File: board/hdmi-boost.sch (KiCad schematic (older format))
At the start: 15 parts, among them P1 PMOD-Device-x2-Type-XHS-Alt, U31 XC9140, U32 REG710-DBV

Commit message: Working on things.
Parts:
- removed P1: PMOD-Device-x2-Type-XHS-Alt, pmod-conn_6x2:pmod_pin_array_6x2, symbol PMOD-Device-x2-Type-XHS-Alt
- added CTX? (x16): 0.1uF, Capacitors_SMD:C_0402, symbol hdmi-boost-rescue:C_Small
- added CTX?: 10n, Capacitors_SMD:C_0402, symbol hdmi-boost-rescue:C_Small
- added CTX? (x4): 0.1uF, Capacitors_SMD:C_0402, symbol hdmi-boost-rescue:C
- added DTX?: D, Diodes_SMD:SOD-523, symbol hdmi-boost-rescue:D
- added J? (x2): HDMI_IN, symbol hdmi-boost-rescue:HDMI_IN
- added JTX? (x2): HDMI_OUT, hdmi:HDMI_TH, symbol hdmi-boost-rescue:HDMI_OUT
- added PTX?: PMOD-CONN_6X2, pmod:pmod_pin_array_6x2, symbol hdmi-boost-rescue:PMOD-CONN_6X2
- added R? (x2): R_Shunt_US, symbol Device:R_Shunt_US
- added RTX?: 27K, Resistors_SMD:R_0402, symbol hdmi-boost-rescue:R
- added RTX? (x4): 2k2, Resistors_SMD:R_0402, symbol hdmi-boost-rescue:R
- added RTX?: 12k4, Resistors_SMD:R_0402, symbol hdmi-boost-rescue:R
- added URX0, UTX0: PTN3363, Housings_DFN_QFN:QFN-32-1EP_5x5mm_Pitch0.5mm, symbol hdmi-boost-rescue:PTN3363
- C311, C322, CV5: symbol C -> hdmi-boost-rescue:C
- C321: symbol C_Small -> hdmi-boost-rescue:C_Small
- L31: symbol INDUCTOR -> hdmi-boost-rescue:INDUCTOR
- R31, R32, RDC1, RDE1, REQ0, REQ1, ROE1: symbol R -> hdmi-boost-rescue:R
- U31: symbol XC9140 -> hdmi-boost-rescue:XC9140
- U32: symbol REG710-DBV -> hdmi-boost-rescue:REG710-DBV
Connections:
- net labels added: HDMIA_RX0_CLK+, HDMIA_RX0_CLK-, HDMIA_RX0_D0+, HDMIA_RX0_D0-, HDMIA_RX0_D1+, HDMIA_RX0_D1-, HDMIA_RX0_D2+, HDMIA_RX0_D2-, HDMIA_TX0_CLK+, HDMIA_TX0_CLK-, HDMIA_TX0_D0+, HDMIA_TX0_D0-, HDMIA_TX0_D1+, HDMIA_TX0_D1-, HDMIA_TX0_D2+, HDMIA_TX0_D2-, HDMIP_RX0_CLK+, HDMIP_RX0_CLK-, HDMIP_RX0_D0+, HDMIP_RX0_D0-, HDMIP_RX0_D1+, HDMIP_RX0_D1-, HDMIP_RX0_D2+, HDMIP_RX0_D2-, HDMIP_RX0_HOT, HDMIP_RX0_SCL, HDMIP_RX0_SDA, HDMIP_TX0_CLK+, HDMIP_TX0_CLK-, HDMIP_TX0_D0+, HDMIP_TX0_D0-, HDMIP_TX0_D1+, HDMIP_TX0_D1-, HDMIP_TX0_D2+, HDMIP_TX0_D2-, HDMIP_TX0_HOT, HDMIP_TX0_SCL, HDMIP_TX0_SDA, HDMI_RX0_CEC, HDMI_TX0_DDC_EN, RX05V0
- wire segments 91 -> 290
- no-connect marks 0 -> 2
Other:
- note added: "Opsis Side"
- note added: "← From Presentor Computer"
- note added: "→ To Long Distance Display"
- note removed: "HDMI High Speed Signals"

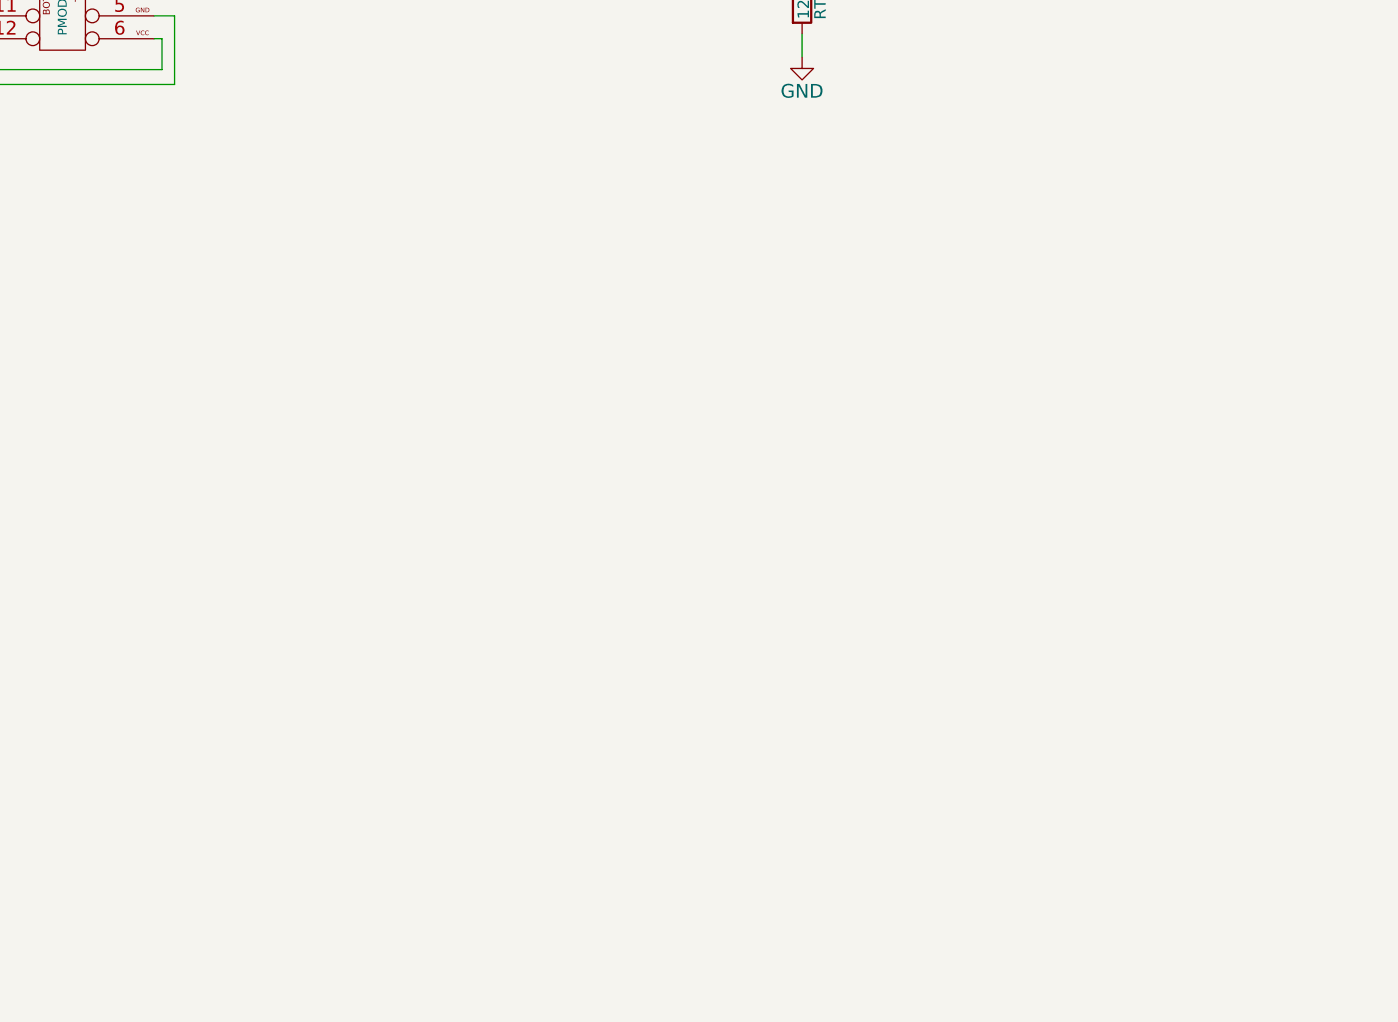
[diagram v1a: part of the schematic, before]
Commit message: Adding efm32hg309 part.
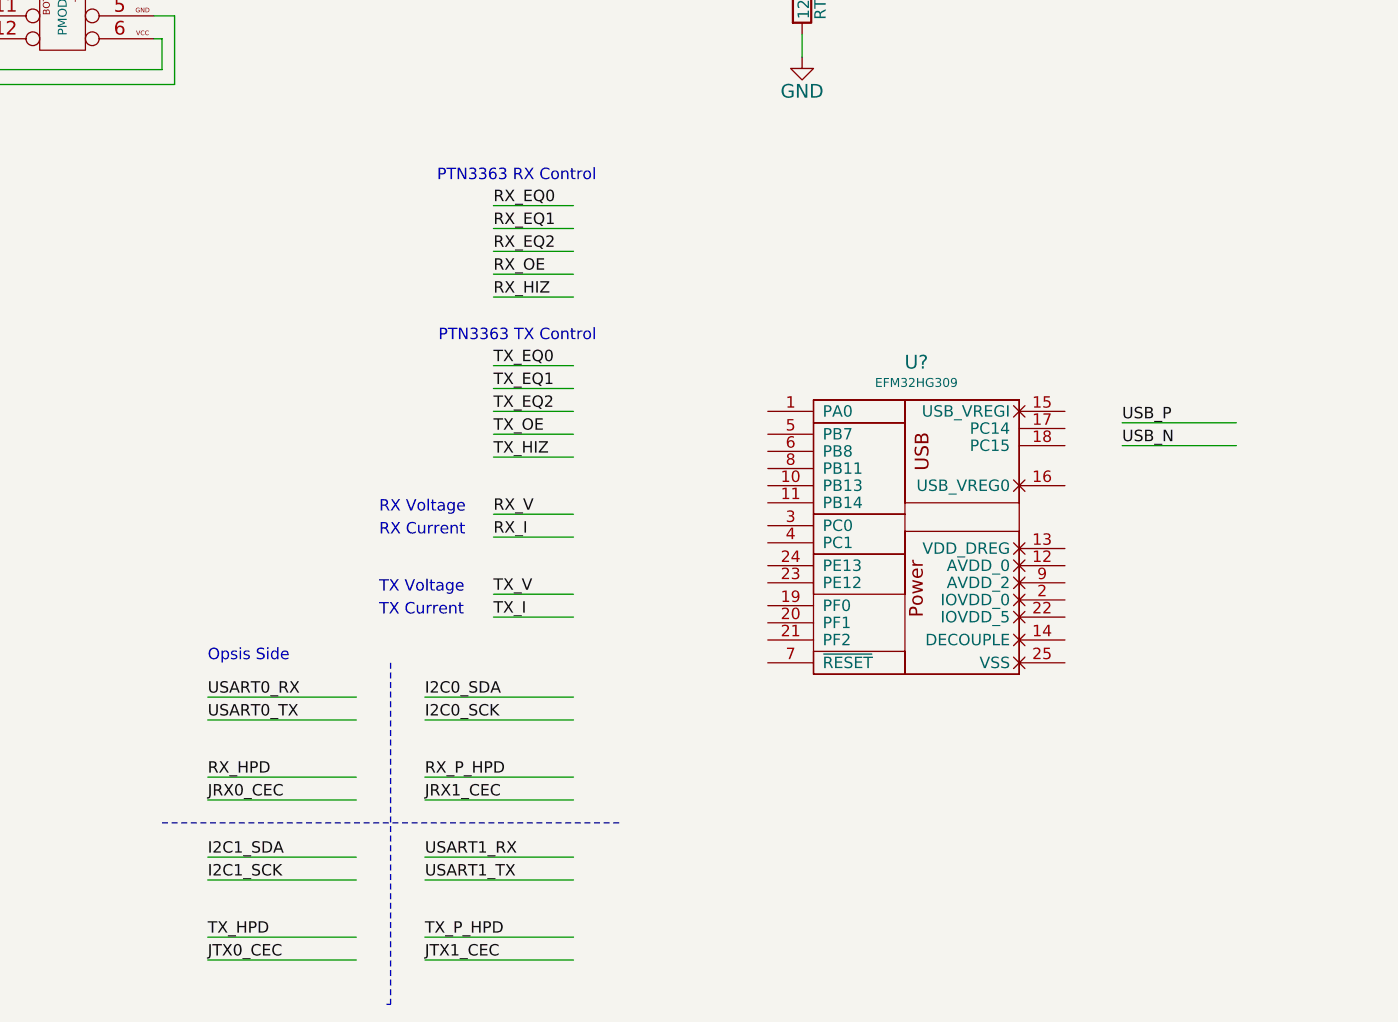
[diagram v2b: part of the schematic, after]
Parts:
- added U?: EFM32HG309, symbol efm32hg309:EFM32HG309
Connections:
- net labels added: I2C0_SCK, I2C0_SDA, I2C1_SCK, I2C1_SDA, JRX0_CEC, JRX1_CEC, JTX0_CEC, JTX1_CEC, RX_EQ0, RX_EQ1, RX_EQ2, RX_HIZ, RX_HPD, RX_I, RX_OE, RX_P_HPD, RX_V, TX_EQ0, TX_EQ1, TX_EQ2, TX_HIZ, TX_HPD, TX_I, TX_OE, TX_P_HPD, TX_V, USART0_RX, USART0_TX, USART1_RX, USART1_TX, USB_N, USB_P
- wire segments 290 -> 322
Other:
- note added: "PTN3363 RX Control"
- note added: "PTN3363 TX Control"
- note added: "RX Current"
- note added: "RX Voltage\n"
- note added: "TX Current"
- note added: "TX Voltage"
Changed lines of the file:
@@
 	25800 8300 25800 8500
 Connection ~ 25800 8300
+$Comp
+L efm32hg309:EFM32HG309 U?
+U 1 1 5E199B4B
+P 16000 8100
+F 0 "U?" H 16450 9465 60  0000 C CNN
+F 1 "EFM32HG309" H 16450 9375 39  0000 C CNN
+F 2 "" H 16000 8100 60  0000 C CNN
+F 3 "" H 16000 8100 60  0000 C CNN
+	1    16000 8100
+	1    0    0    -1
+$EndComp
+Wire Wire Line
+	14000 8200 13350 8200
+Wire Wire Line
+	14000 8300 13350 8300
+Text Label 13350 8200 0    50   ~ 0
+USART0_RX
+Text Label 13350 8300 0    50   ~ 0
+USART0_TX
+Wire Wire Line
+	14950 8900 14300 8900
+Wire Wire Line
+	14300 9000 14950 9000
+Text Label 14300 8900 0    50   ~ 0
+USART1_RX
+Text Label 14300 9000 0    50   ~ 0
+USART1_TX
+Wire Wire Line
+	14950 8200 14300 8200
+Wire Wire Line
+	14300 8300 14950 8300
+Wire Wire Line
+	14000 8900 13350 8900
+Wire Wire Line
+	13350 9000 14000 9000
+Text Label 14300 8200 0    50   ~ 0
+I2C0_SDA
+Text Label 14300 8300 0    50   ~ 0
+I2C0_SCK
+Text Label 13350 8900 0    50   ~ 0
+I2C1_SDA
+Text Label 13350 9000 0    50   ~ 0
+I2C1_SCK
+Wire Wire Line
+	17350 7000 17850 7000
+Wire Wire Line
+	17350 7100 17850 7100
+Text Label 17350 7000 0    50   ~ 0
+USB_P
+Text Label 17350 7100 0    50   ~ 0
+USB_N
+Wire Wire Line
+	14950 7400 14600 7400
+Wire Wire Line
+	14600 7500 14950 7500
+Wire Wire Line
+	14600 7750 14950 7750
+Wire Wire Line
+	14600 7850 14950 7850
+Text Label 14600 7400 0    50   ~ 0
+RX_V
+Text Label 14600 7500 0    50   ~ 0
+RX_I
+Text Label 14600 7750 0    50   ~ 0
+TX_V
+Text Label 14600 7850 0    50   ~ 0
+TX_I
+Wire Wire Line
+	14950 6950 14600 6950
+Wire Wire Line
+	14600 6850 14950 6850
+Wire Wire Line
+	14950 6750 14600 6750
+Wire Wire Line
+	14950 6250 14600 6250
+Wire Wire Line
+	14950 6150 14600 6150
+Wire Wire Line
+	14950 6050 14600 6050
+Text Label 14600 6750 0    50   ~ 0
+TX_EQ0
+Text Label 14600 6850 0    50   ~ 0
+TX_EQ1
+Text Label 14600 6950 0    50   ~ 0
+TX_EQ2
+Text Label 14600 6050 0    50   ~ 0
+RX_EQ0
+Text Label 14600 6150 0    50   ~ 0
+RX_EQ1
+Text Label 14600 6250 0    50   ~ 0
+RX_EQ2
+Wire Wire Line
+	13350 8550 14000 8550
+Wire Wire Line
+	13350 9250 14000 9250
+Text Label 13350 8550 0    50   ~ 0
+RX_HPD
+Text Label 13350 9250 0    50   ~ 0
+TX_HPD
+Wire Wire Line
+	14300 8550 14950 8550
+Wire Wire Line
+	14300 9250 14950 9250
+Text Label 14300 8550 0    50   ~ 0
+RX_P_HPD
+Text Label 14300 9250 0    50   ~ 0
+TX_P_HPD
+Wire Wire Line
+	14950 6350 14600 6350
+Wire Wire Line
+	14950 7050 14600 7050
+Text Label 14600 6350 0    50   ~ 0
+RX_OE
+Text Label 14600 7050 0    50   ~ 0
+TX_OE
+Wire Wire Line
+	14950 6450 14600 6450
+Wire Wire Line
+	14600 7150 14950 7150
+Text Label 14600 6450 0    50   ~ 0
+RX_HIZ
+Text Label 14600 7150 0    50   ~ 0
+TX_HIZ
+Wire Wire Line
+	14000 8650 13350 8650
+Wire Wire Line
+	14950 9350 14300 9350
+Wire Wire Line
+	14950 8650 14300 8650
+Wire Wire Line
+	13350 9350 14000 9350
+Text Label 13350 8650 0    50   ~ 0
+JRX0_CEC
+Text Label 14300 8650 0    50   ~ 0
+JRX1_CEC
+Text Label 13350 9350 0    50   ~ 0
+JTX0_CEC
+Text Label 14300 9350 0    50   ~ 0
+JTX1_CEC
+Text Notes 14100 7400 0    50   ~ 0
+RX Voltage\n
+Text Notes 14100 7500 0    50   ~ 0
+RX Current
+Text Notes 14100 7750 0    50   ~ 0
+TX Voltage
+Text Notes 14100 7850 0    50   ~ 0
+TX Current
+Text Notes 15050 5950 2    50   ~ 0
+PTN3363 RX Control
+Text Notes 15050 6650 2    50   ~ 0
+PTN3363 TX Control
+Wire Notes Line
+	14150 8050 14150 9544
+Wire Notes Line
+	14150 9544 14132 9544
+Text Notes 13350 8050 0    50   ~ 0
+Opsis Side
+Wire Notes Line
+	15150 8750 13150 8750
 $EndSCHEMATC

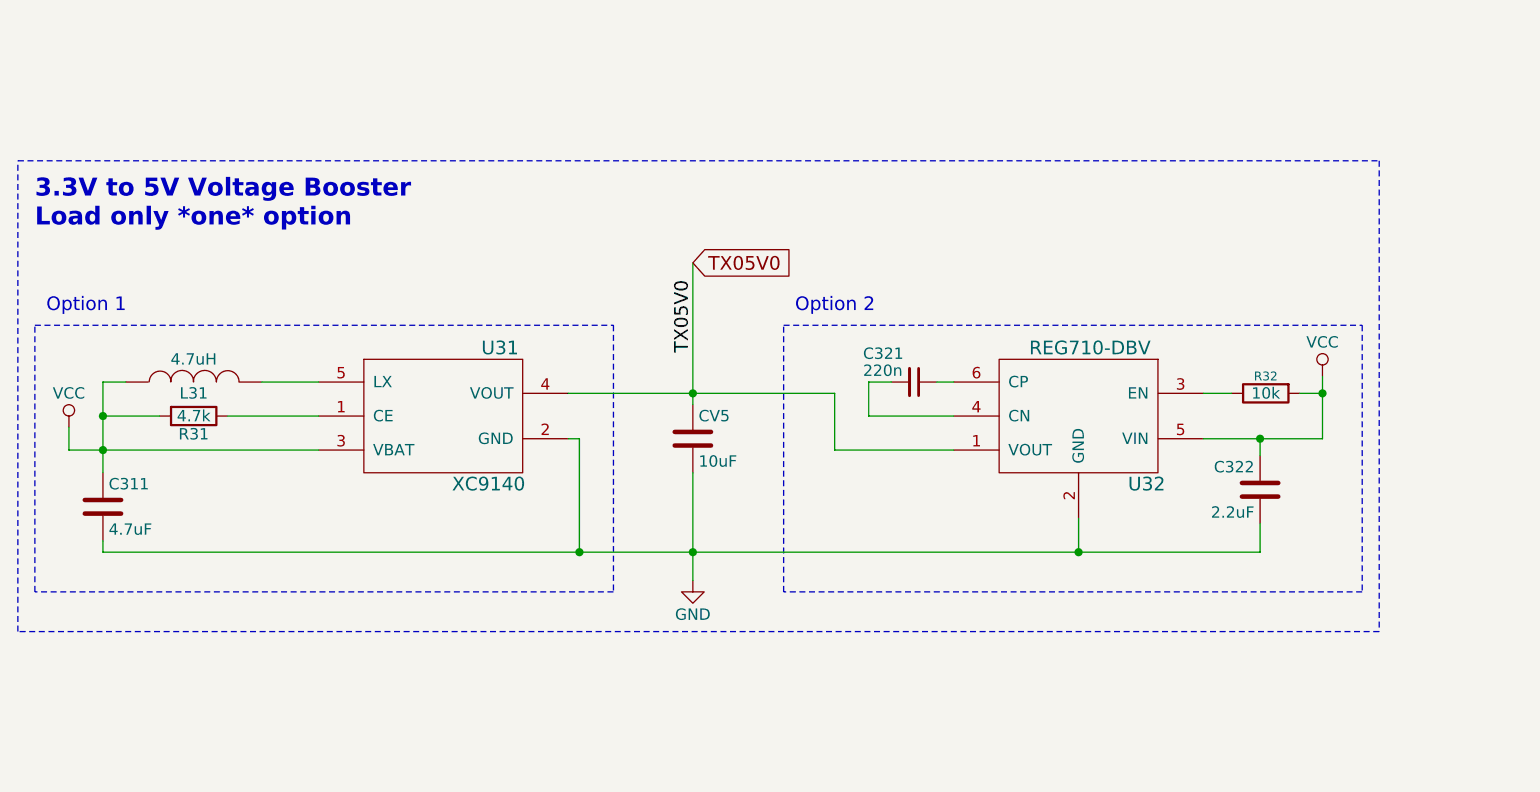
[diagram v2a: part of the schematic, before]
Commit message: Remove 3V3->5V converters.
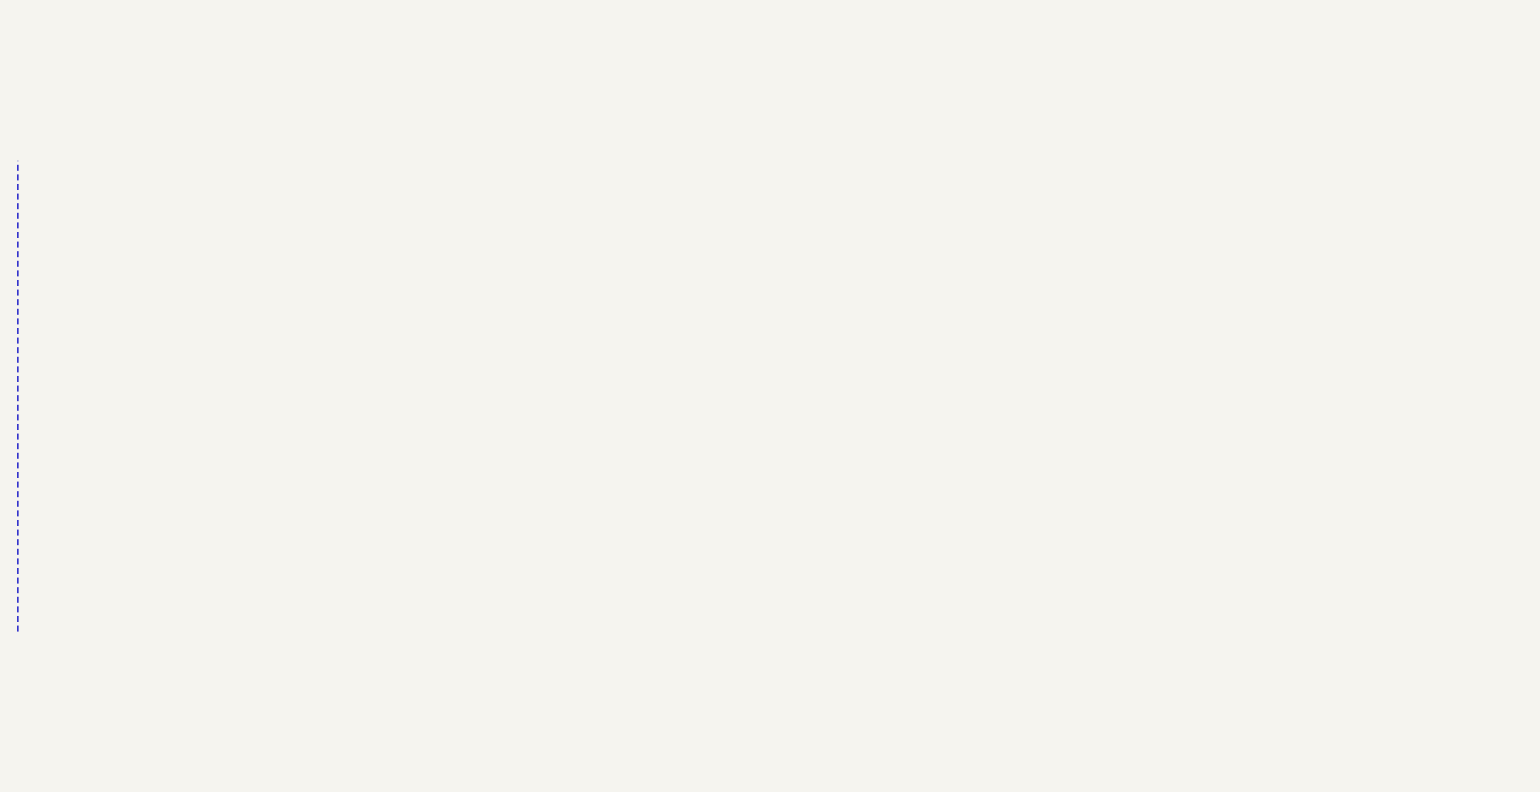
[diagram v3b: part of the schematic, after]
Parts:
- removed C311: 4.7uF, Capacitors_SMD:C_0603, symbol hdmi-boost-rescue:C
- removed C321: 220n, Capacitors_SMD:C_0402, symbol hdmi-boost-rescue:C_Small
- removed C322: 2.2uF, Capacitors_SMD:C_0603, symbol hdmi-boost-rescue:C
- removed CV5: 10uF, Capacitors_SMD:C_1206, symbol hdmi-boost-rescue:C
- removed L31: 4.7uH, Inductors_NEOSID:Neosid_Inductor_SM0603CG, symbol hdmi-boost-rescue:INDUCTOR
- removed R31: 4.7k, Resistors_SMD:R_0402, symbol hdmi-boost-rescue:R
- removed R32: 10k, Resistors_SMD:R_0402, symbol hdmi-boost-rescue:R
- removed U31: XC9140, TO_SOT_Packages_SMD:SOT-23-5, symbol hdmi-boost-rescue:XC9140
- removed U32: REG710-DBV, TO_SOT_Packages_SMD:SOT-23-6, symbol hdmi-boost-rescue:REG710-DBV
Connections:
- wire segments 322 -> 284
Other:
- note removed: "3.3V to 5V Voltage Booster\nLoad only *one* option\n"
- note removed: "Option 1\n"
- note removed: "Option 2"
